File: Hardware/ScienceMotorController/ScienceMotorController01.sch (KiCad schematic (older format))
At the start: 7 parts, among them U1 LM2576D2TR4

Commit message: finished arranging components
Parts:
- D3: footprint Diode_SMD:D_0603_1608Metric_Pad1.05x0.95mm_HandSolder -> Diode_THT:D_DO-201AD_P15.24mm_Horizontal
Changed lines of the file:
@@
 F 0 "D3" V 4200 2200 50  0000 R CNN
 F 1 "D_Schottky_Small" V 4100 2650 50  0000 R CNN
-F 2 "Diode_SMD:D_0603_1608Metric_Pad1.05x0.95mm_HandSolder" V 4100 2000 50  0001 C CNN
+F 2 "Diode_THT:D_DO-201AD_P15.24mm_Horizontal" V 4100 2000 50  0001 C CNN
 F 3 "~" V 4100 2000 50  0001 C CNN
 	1    4100 2000

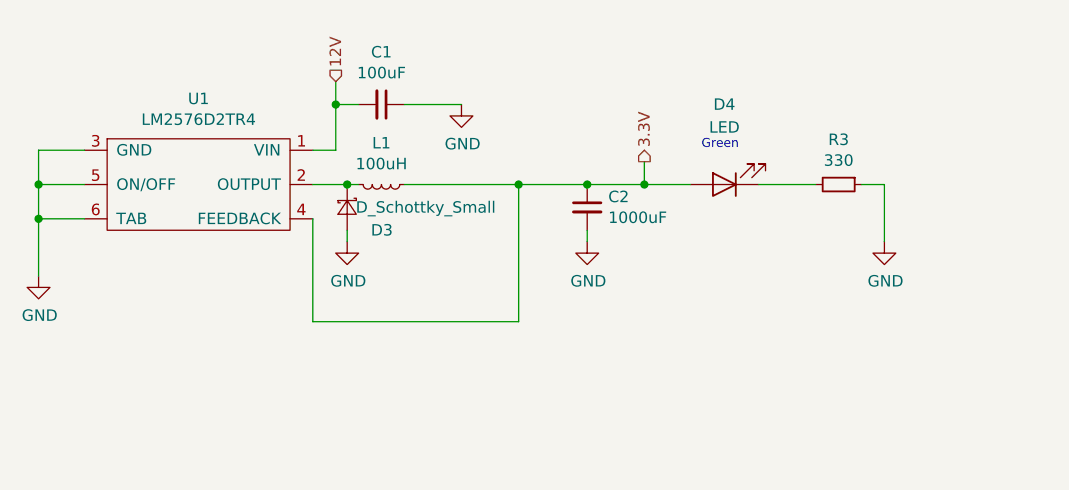
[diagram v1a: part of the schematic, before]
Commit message: added oki and began rerouting traces
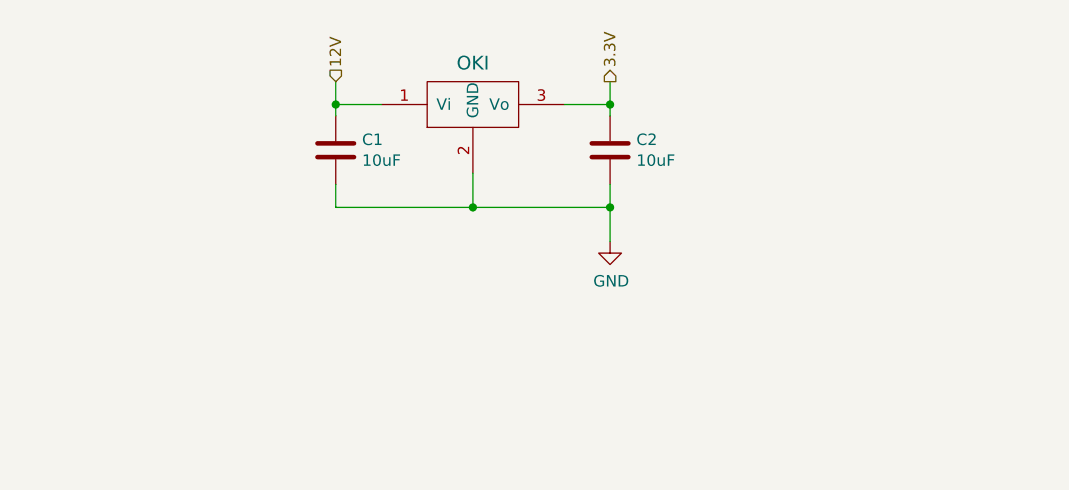
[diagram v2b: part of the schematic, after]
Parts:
- removed C1: 100uF, Capacitor_SMD:C_0603_1608Metric_Pad1.05x0.95mm_HandSolder, symbol Device:C_Small
- removed C2: 1000uF, Capacitor_SMD:C_0603_1608Metric_Pad1.05x0.95mm_HandSolder, symbol Device:C_Small
- removed D3: D_Schottky_Small, Diode_THT:D_DO-201AD_P15.24mm_Horizontal, symbol Device:D_Schottky_Small
- removed D4: LED, LED_SMD:LED_0603_1608Metric_Pad1.05x0.95mm_HandSolder, symbol Device:LED
- removed L1: 100uH, Inductor_SMD:L_0603_1608Metric_Pad1.05x0.95mm_HandSolder, symbol Device:L_Small
- removed R3: 330, Resistor_SMD:R_0603_1608Metric_Pad1.05x0.95mm_HandSolder, symbol Device:R_Small
- removed U1: LM2576D2TR4, MRDT_Devices:LM2576, symbol MRDT_Devices:LM2576D2TR4
- added C1, C2: 10uF, Capacitor_SMD:C_0603_1608Metric_Pad1.05x0.95mm_HandSolder, symbol Device:C
- added U1: OKI, MRDT_Devices:OKI_Horizontal, symbol MRDT_Devices:OKI
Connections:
- net 12V: now also C1.1, U1.1 (Vi)
- net 3.3V: now also C2.1, U1.3 (Vo)
- net GND: now also C1.2, C2.2, U1.2 (GND)
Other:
- note removed: "Green"
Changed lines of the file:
@@
 Text Notes 7100 7000 0    315  ~ 0
 Sheet 01: Power
+Text HLabel 5250 1450 1    50   Output ~ 0
+3.3V
+Text HLabel 4050 1450 1    50   Input ~ 0
+12V
 $Comp
-L MRDT_Devices:LM2576D2TR4 U1
-U 1 1 5F6E48CD
-P 3450 1950
-F 0 "U1" H 3450 2375 50  0000 C CNN
-F 1 "LM2576D2TR4" H 3450 2284 50  0000 C CNN
-F 2 "MRDT_Devices:LM2576" H 3450 2400 50  0001 C CNN
-F 3 "https://www.mouser.com/datasheet/2/308/LM2576_D-1810688.pdf" H 3450 2400 50  0001 C CNN
-	1    3450 1950
+L MRDT_Devices:OKI U1
+U 1 1 5FBF8B08
+P 4450 1650
+F 0 "U1" H 4500 1600 60  0001 C CNN
+F 1 "OKI" H 4650 1931 60  0000 C CNN
+F 2 "MRDT_Devices:OKI_Horizontal" H 4250 1550 60  0001 C CNN
+F 3 "" H 4250 1550 60  0001 C CNN
+	1    4450 1650
 	1    0    0    -1
 $EndComp
 Wire Wire Line
-	2950 1750 2750 1750
+	5050 1550 5250 1550
 Wire Wire Line
-	2750 1750 2750 1900
-Wire Wire Line
-	2950 1900 2750 1900
-Connection ~ 2750 1900
-Wire Wire Line
-	2750 1900 2750 2050
-Wire Wire Line
-	2950 2050 2750 2050
-Connection ~ 2750 2050
-Wire Wire Line
-	2750 2050 2750 2300
+	4250 1550 4050 1550
 $Comp
-L power:GND #PWR05
-U 1 1 5F6EE7DC
-P 2750 2300
-F 0 "#PWR05" H 2750 2050 50  0001 C CNN
-F 1 "GND" H 2755 2127 50  0000 C CNN
-F 2 "" H 2750 2300 50  0001 C CNN
-F 3 "" H 2750 2300 50  0001 C CNN
-	1    2750 2300
+L Device:C C1
+U 1 1 5FBF8B10
+P 4050 1750
+F 0 "C1" H 4165 1796 50  0000 L CNN
+F 1 "10uF" H 4165 1705 50  0000 L CNN
+F 2 "Capacitor_SMD:C_0603_1608Metric_Pad1.05x0.95mm_HandSolder" H 4088 1600 50  0001 C CNN
+F 3 "~" H 4050 1750 50  0001 C CNN
+	1    4050 1750
 	1    0    0    -1
 $EndComp
 $Comp
-L power:GND #PWR07
-U 1 1 5F6EFF75
-P 4600 1550
-F 0 "#PWR07" H 4600 1300 50  0001 C CNN
-F 1 "GND" H 4605 1377 50  0000 C CNN
-F 2 "" H 4600 1550 50  0001 C CNN
-F 3 "" H 4600 1550 50  0001 C CNN
-	1    4600 1550
-	1    0    0    -1
-$EndComp
-$Comp
-L Device:C_Small C1
-U 1 1 5F6F25A2
-P 4250 1550
-F 0 "C1" V 4021 1550 50  0000 C CNN
-F 1 "100uF" V 4112 1550 50  0000 C CNN
-F 2 "Capacitor_SMD:C_0603_1608Metric_Pad1.05x0.95mm_HandSolder" H 4250 1550 50  0001 C CNN
-F 3 "~" H 4250 1550 50  0001 C CNN
-	1    4250 1550
-	0    1    1    0
-$EndComp
-Wire Wire Line
-	4350 1550 4600 1550
-$Comp
-L Device:L_Small L1
-U 1 1 5F6FA71E
-P 4250 1900
-F 0 "L1" V 4069 1900 50  0000 C CNN
-F 1 "100uH" V 4160 1900 50  0000 C CNN
-F 2 "Inductor_SMD:L_0603_1608Metric_Pad1.05x0.95mm_HandSolder" H 4250 1900 50  0001 C CNN
-F 3 "~" H 4250 1900 50  0001 C CNN
-	1    4250 1900
-	0    1    1    0
-$EndComp
-Wire Wire Line
-	4050 1450 4050 1550
-Wire Wire Line
-	4050 1750 3950 1750
-Wire Wire Line
-	4150 1550 4050 1550
-Connection ~ 4050 1550
-Wire Wire Line
-	4050 1550 4050 1750
-$Comp
-L power:GND #PWR06
-U 1 1 5F7020BE
-P 4100 2150
-F 0 "#PWR06" H 4100 1900 50  0001 C CNN
-F 1 "GND" H 4105 1977 50  0000 C CNN
-F 2 "" H 4100 2150 50  0001 C CNN
-F 3 "" H 4100 2150 50  0001 C CNN
-	1    4100 2150
+L Device:C C2
+U 1 1 5FBF8B16
+P 5250 1750
+F 0 "C2" H 5365 1796 50  0000 L CNN
+F 1 "10uF" H 5365 1705 50  0000 L CNN
+F 2 "Capacitor_SMD:C_0603_1608Metric_Pad1.05x0.95mm_HandSolder" H 5288 1600 50  0001 C CNN
+F 3 "~" H 5250 1750 50  0001 C CNN
+	1    5250 1750
 	1    0    0    -1
 $EndComp
 Wire Wire Line
-	4100 2100 4100 2150
+	4050 1900 4050 2000
+Wire Wire Line
+	4050 2000 4650 2000
+Wire Wire Line
+	5250 2000 5250 1900
+Wire Wire Line
+	4650 1850 4650 2000
+Connection ~ 4650 2000
+Wire Wire Line
+	5250 1600 5250 1550
+Wire Wire Line
+	4050 1600 4050 1550
+Wire Wire Line
+	5250 1450 5250 1550
+Connection ~ 5250 1550
+Wire Wire Line
+	4050 1450 4050 1550
+Connection ~ 4050 1550
 $Comp
-L Device:C_Small C2
-U 1 1 5F702EE3
-P 5150 2000
-F 0 "C2" H 5242 2046 50  0000 L CNN
-F 1 "1000uF" H 5242 1955 50  0000 L CNN
-F 2 "Capacitor_SMD:C_0603_1608Metric_Pad1.05x0.95mm_HandSolder" H 5150 2000 50  0001 C CNN
-F 3 "~" H 5150 2000 50  0001 C CNN
-	1    5150 2000
-	1    0    0    -1
-$EndComp
-$Comp
-L power:GND #PWR08
-U 1 1 5F70490E
-P 5150 2150
-F 0 "#PWR08" H 5150 1900 50  0001 C CNN
-F 1 "GND" H 5155 1977 50  0000 C CNN
-F 2 "" H 5150 2150 50  0001 C CNN
-F 3 "" H 5150 2150 50  0001 C CNN
-	1    5150 2150
+L power:GND #PWR05
+U 1 1 5FBF941F
+P 5250 2150
+F 0 "#PWR05" H 5250 1900 50  0001 C CNN
+F 1 "GND" H 5255 1977 50  0000 C CNN
+F 2 "" H 5250 2150 50  0001 C CNN
+F 3 "" H 5250 2150 50  0001 C CNN
+	1    5250 2150
 	1    0    0    -1
 $EndComp
 Wire Wire Line
-	5150 2100 5150 2150
+	4650 2000 5250 2000
 Wire Wire Line
-	3950 2050 3950 2500
-Wire Wire Line
-	3950 2500 4850 2500
-Wire Wire Line
-	4850 2500 4850 1900
-Wire Wire Line
-	4850 1900 4350 1900
-Wire Wire Line
-	5150 1900 4850 1900
-Connection ~ 4850 1900
-Wire Wire Line
-	5400 1900 5150 1900
-Connection ~ 5150 1900
-Wire Wire Line
-	5400 1800 5400 1900
-$Comp
-L Device:LED D4
-U 1 1 5F70C395
-P 5750 1900
-F 0 "D4" H 5750 1550 50  0000 C CNN
-F 1 "LED" H 5750 1650 50  0000 C CNN
-F 2 "LED_SMD:LED_0603_1608Metric_Pad1.05x0.95mm_HandSolder" H 5750 1900 50  0001 C CNN
-F 3 "~" H 5750 1900 50  0001 C CNN
-	1    5750 1900
-	-1   0    0    1
-$EndComp
-Wire Wire Line
-	5400 1900 5600 1900
-Connection ~ 5400 1900
-Text Notes 5650 1750 0    39   ~ 0
-Green
-Wire Wire Line
-	5900 1900 6150 1900
-$Comp
-L Device:R_Small R3
-U 1 1 5F7119AC
-P 6250 1900
-F 0 "R3" V 6054 1900 50  0000 C CNN
-F 1 "330" V 6145 1900 50  0000 C CNN
-F 2 "Resistor_SMD:R_0603_1608Metric_Pad1.05x0.95mm_HandSolder" H 6250 1900 50  0001 C CNN
-F 3 "~" H 6250 1900 50  0001 C CNN
-	1    6250 1900
-	0    1    1    0
-$EndComp
-$Comp
-L power:GND #PWR09
-U 1 1 5F712ED5
-P 6450 2150
-F 0 "#PWR09" H 6450 1900 50  0001 C CNN
-F 1 "GND" H 6455 1977 50  0000 C CNN
-F 2 "" H 6450 2150 50  0001 C CNN
-F 3 "" H 6450 2150 50  0001 C CNN
-	1    6450 2150
-	1    0    0    -1
-$EndComp
-Wire Wire Line
-	6350 1900 6450 1900
-Wire Wire Line
-	6450 1900 6450 2150
-$Comp
-L Device:D_Schottky_Small D3
-U 1 1 5F80E7DD
-P 4100 2000
-F 0 "D3" V 4200 2200 50  0000 R CNN
-F 1 "D_Schottky_Small" V 4100 2650 50  0000 R CNN
-F 2 "Diode_THT:D_DO-201AD_P15.24mm_Horizontal" V 4100 2000 50  0001 C CNN
-F 3 "~" V 4100 2000 50  0001 C CNN
-	1    4100 2000
-	0    1    1    0
-$EndComp
-Wire Wire Line
-	3950 1900 4100 1900
-Connection ~ 4100 1900
-Wire Wire Line
-	4100 1900 4150 1900
-Text HLabel 4050 1450 1    50   Input ~ 0
-12V
-Text HLabel 5400 1800 1    50   Output ~ 0
-3.3V
+	5250 2150 5250 2000
+Connection ~ 5250 2000
 $EndSCHEMATC
